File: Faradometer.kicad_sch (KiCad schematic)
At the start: 20 parts, among them U1 ${SIM.PARAMS}, U2 ${SIM.PARAMS}, U3 ${SIM.PARAMS}, U4 ${SIM.PARAMS}

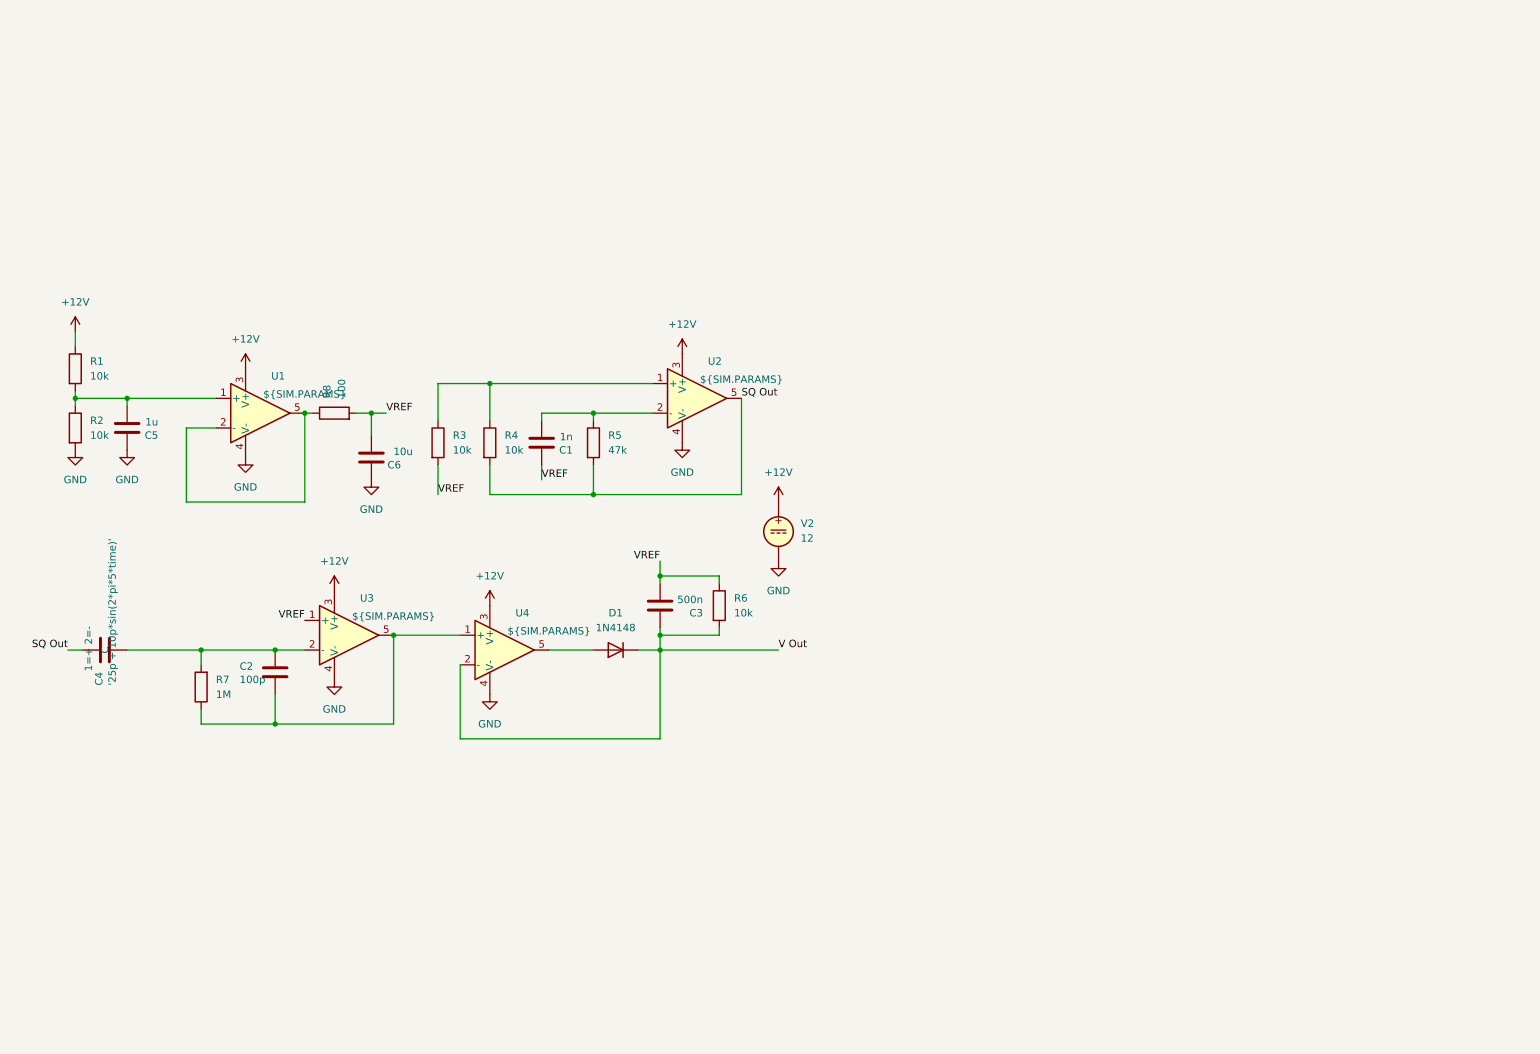
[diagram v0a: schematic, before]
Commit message: change the symbols in schematic and made the pcb wirings
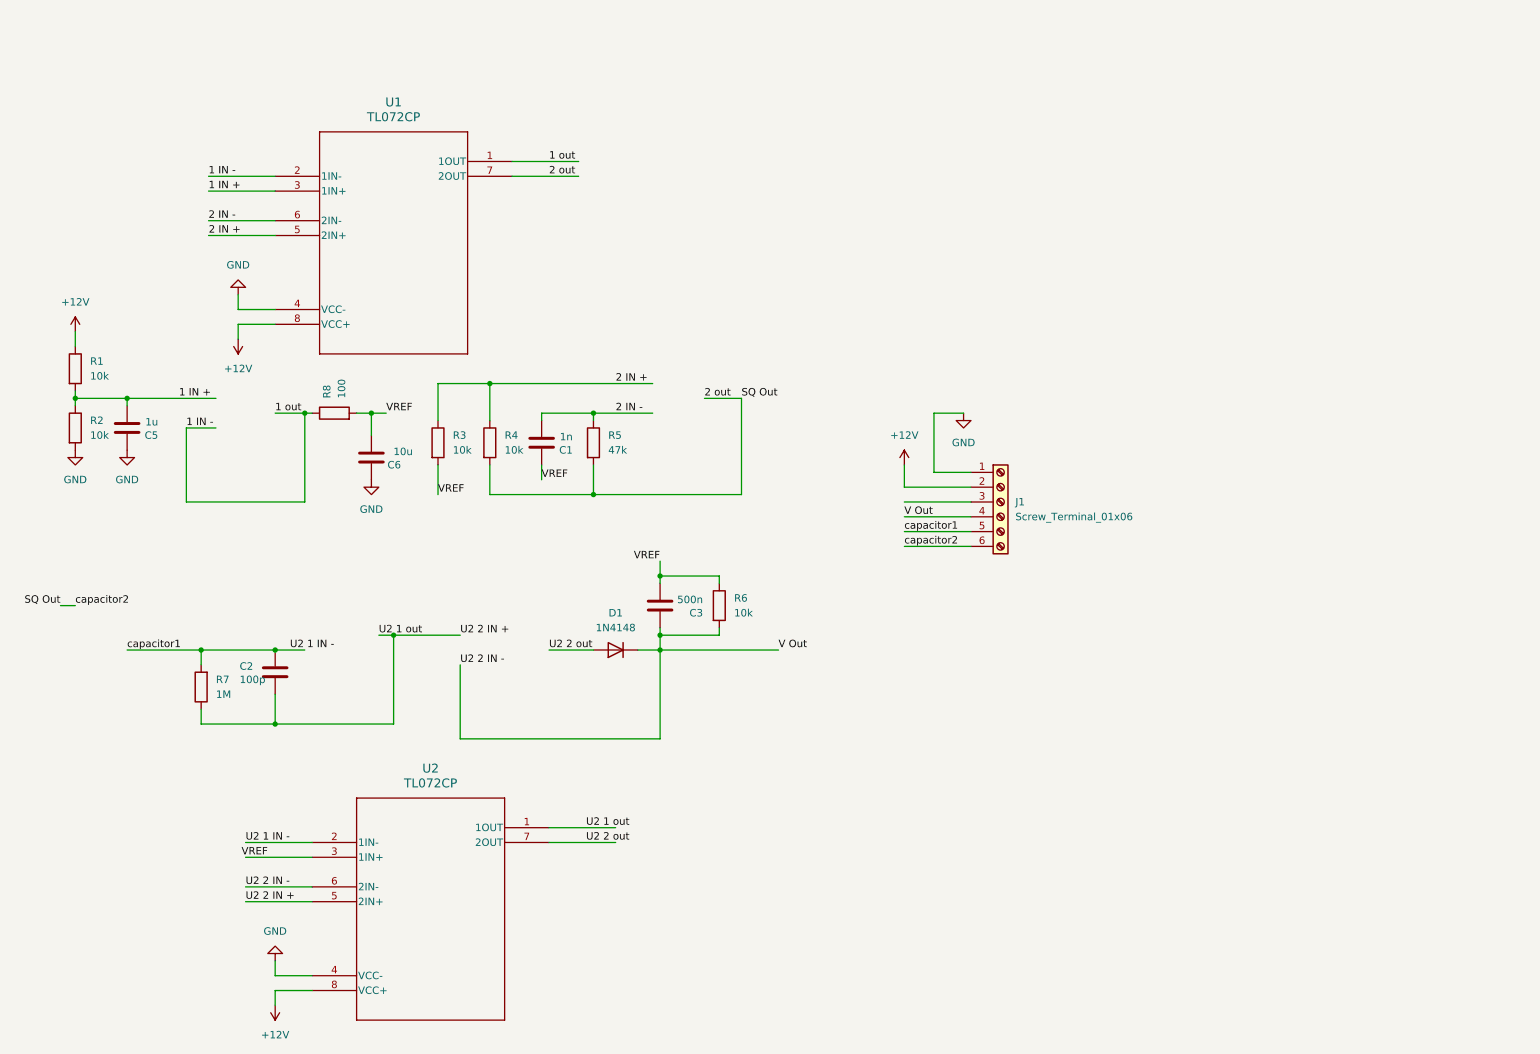
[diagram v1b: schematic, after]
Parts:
- removed C4: '25p + 10p*sin(2*pi*5*time)', symbol Device:C
- removed U1, U2, U3, U4: ${SIM.PARAMS}, symbol Simulation_SPICE:OPAMP
- removed V2: 12, symbol Simulation_SPICE:VDC
- added J1: Screw_Terminal_01x06, Screw Terminal x6:TE_282836-6, symbol Connector:Screw_Terminal_01x06
- added U1, U2: TL072CP, TL072CP:P8, symbol TL072CP:TL072CP
- C1, C2, C3, C5, C6: footprint (none) -> Capacitor_SMD:C_0805_2012Metric
- R1, R2, R3, R4, R5, R6, R7, R8: footprint (none) -> Resistor_SMD:R_0805_2012Metric
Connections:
- net +12V: now also J1.2 (Pin_2), U1.8 (VCC+), U2.8 (VCC+)
- net GND: now also J1.1 (Pin_1), U1.4 (VCC-), U2.4 (VCC-)
- net VREF: now also U2.3 (1IN+)
- net U2 2 out: now reaches D1.2 (A)
- net U2 2 out: now also U2.7 (2OUT)
- net U2 1 out: now reaches C2.2, R7.1
- net U2 1 out: now also U2.1 (1OUT), U2.5 (2IN+)
- net 2 IN +: now reaches R3.1, R4.1
- net 2 IN +: now also U1.5 (2IN+)
- net U2 1 IN -: now reaches C2.1, R7.2
- net U2 1 IN -: now also J1.5 (Pin_5), U2.2 (1IN-)
- net 1 IN +: now reaches C5.2, R1.2, R2.1
- net 1 IN +: now also U1.3 (1IN+)
- net 2 IN -: now reaches C1.2, R5.1
- net 2 IN -: now also U1.6 (2IN-)
- net 1 IN -: now reaches R8.1
- net 1 IN -: now also U1.1 (1OUT), U1.2 (1IN-)
- net SQ Out renamed 2 out
- net 2 out: now also J1.6 (Pin_6), U1.7 (2OUT)
- net V Out renamed U2 2 IN -
- net U2 2 IN -: now also J1.4 (Pin_4), U2.6 (2IN-)

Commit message: Describe what you changed
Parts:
- removed J1: Screw_Terminal_01x06, Screw Terminal x6:TE_282836-6, symbol Connector:Screw_Terminal_01x06
- added H1, H2: MountingHole_Pad, MountingHole:MountingHole_3.2mm_M3_DIN965_Pad, symbol Mechanical:MountingHole_Pad
- added J3: Conn_01x02_Pin, Connector_Molex:Molex_Nano-Fit_105313-xx02_1x02_P2.50mm_Horizontal, symbol Connector:Conn_01x02_Pin
- added J4: Conn_01x03_Pin, Connector_Molex:Molex_Nano-Fit_105313-xx03_1x03_P2.50mm_Horizontal, symbol Connector:Conn_01x03_Pin
- C1, C2, C3: footprint Capacitor_SMD:C_0805_2012Metric -> Capacitor_SMD:C_0402_1005Metric_Pad0.74x0.62mm_HandSolder
- C5: footprint Capacitor_SMD:C_0805_2012Metric -> Capacitor_SMD:C_0603_1608Metric_Pad1.08x0.95mm_HandSolder
- C6: footprint Capacitor_SMD:C_0805_2012Metric -> Capacitor_SMD:C_0805_2012Metric_Pad1.18x1.45mm_HandSolder
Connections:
- net +12V: now also J4.1 (Pin_1)
- net 2 out: now also J3.2 (Pin_2)
- net GND: now also H1.1, H2.1, J4.2 (Pin_2)
- net U2 1 IN -: now also J3.1 (Pin_1)
- net U2 2 IN -: now also J4.3 (Pin_3)
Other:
- moved on the sheet: U1

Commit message: annotated schematic
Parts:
- removed U1, U2: TL072CP, TL072CP:P8, symbol TL072CP:TL072CP
- added U101, U102: TL072CP, Package_DIP:DIP-8_W7.62mm, symbol ICLR_HW:TL072CP
- renumbered C5 to C101, C2 to C102, C6 to C103, C1 to C104, C3 to C105, D1 to D101, H2 to H101, H1 to H102, J3 to J101, J4 to J102, R1 to R101, R2 to R102, R7 to R103, R8 to R104, R3 to R105, R4 to R106, R5 to R107, R6 to R108
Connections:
- net +12V: now also U101.8 (VCC+), U102.8 (VCC+)
- net GND: now also U101.4 (VCC-), U102.4 (VCC-)
- net VREF: now also U102.3 (+)
- net 1 IN +: no longer names the net of C101.2, R101.2, R102.1
- net 1 IN +: now also U101.3 (+)
- net 1 IN -: no longer names the net of R104.1
- net 1 IN -: now also U101.1, U101.2 (-)
- net 2 IN +: no longer names the net of R105.1, R106.1
- net 2 IN +: now also U101.5 (+)
- net 2 IN -: no longer names the net of C104.2, R107.1
- net 2 IN -: now also U101.6 (-)
- net 2 out renamed SQ Out
- net SQ Out: now also U101.7
- net U2 1 IN - renamed capacitor1
- net capacitor1: now also U102.2 (-)
- net U2 1 out: no longer names the net of C102.2, R103.1
- net U2 1 out: now also U102.1, U102.5 (+)
- net U2 2 IN - renamed V Out
- net V Out: now also U102.6 (-)
- net U2 2 out: no longer names the net of D101.2 (A)
- net U2 2 out: now also U102.7
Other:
- note added: "Buffered voltage reference"
- note added: "Capacitive fill sensor"
- note added: "Charge amplifier"
- note added: "Precision peak detector"
- note added: "Square wave generator"
- moved on the sheet: C101, C102, C103, C104, C105, D101, H101, H102, J101, J102, R101, R102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
